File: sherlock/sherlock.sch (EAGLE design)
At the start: 24 parts, among them U3 XBEE-1B2, X1 2540-

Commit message: Fix all schematics to have a frame and be in quadrant I
Change-Id: I9709ffe2e940512e8f74172f888a837b658cad74
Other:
- moved on the sheet: BATTBUZZ, BATTCONN, C1, C2, C3, IC1, LED1, LED2, LED3, LED4, P1, P2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

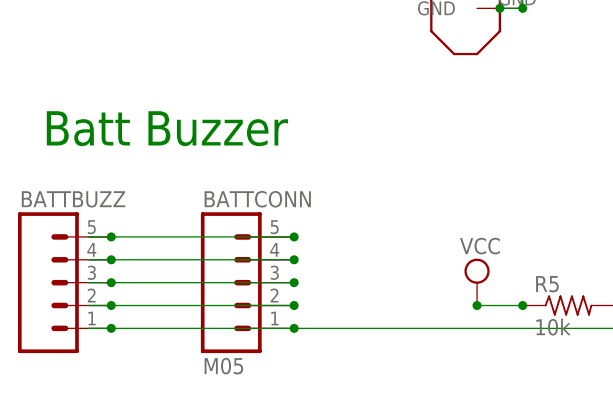
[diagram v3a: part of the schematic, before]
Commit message: Fixed XT60 connector in pie.lbr. Changed battery connector on sherlock to have 4 pins instead of 5. Replaced XT60 on sherlock, solenoid board, and grizzly bear with new version.
Change-Id: Ic4b688068eb477e37db8d2c4f2efb7678e25c5b6
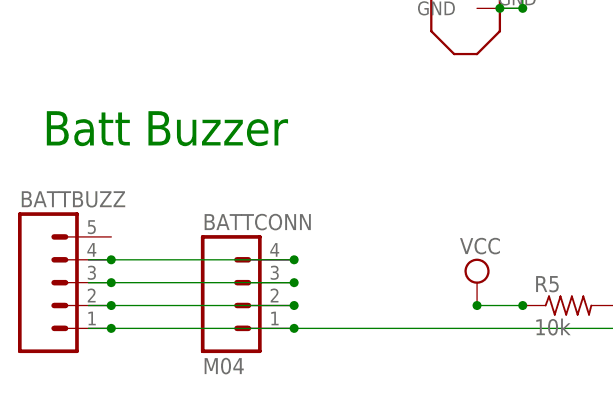
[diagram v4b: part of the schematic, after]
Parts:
- BATTCONN: value M05 -> M04; device pie:M05 -> pie:M04
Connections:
- removed net N$4: BATTBUZZ.5, BATTCONN.5
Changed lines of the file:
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@@
 <?xml version="1.0" encoding="utf-8"?>
 <!DOCTYPE eagle SYSTEM "eagle.dtd">
-<eagle version="6.2">
+<eagle version="6.3">
 <drawing>
 <settings>
@@
 </part>
 <part name="U$1" library="pie" deviceset="XT60CONNECTOR" device=""/>
-<part name="BATTCONN" library="pie" deviceset="M05" device=""/>
+<part name="BATTCONN" library="pie" deviceset="M04" device=""/>
 <part name="BATTBUZZ" library="SparkFun" deviceset="M05" device="PTH"/>
 <part name="R5" library="resistor" deviceset="R-US_" device="R0603" value="10k"/>
@@
 <instance part="X1" gate="-40" x="12.7" y="170.18" rot="R270"/>
 <instance part="U$1" gate="G$1" x="55.88" y="60.96" rot="R270"/>
-<instance part="BATTCONN" gate="G$1" x="35.56" y="22.86"/>
+<instance part="BATTCONN" gate="G$1" x="35.56" y="20.32"/>
 <instance part="BATTBUZZ" gate="G$1" x="12.7" y="20.32"/>
 <instance part="R5" gate="G$1" x="71.12" y="17.78"/>
@@
 </segment>
 </net>
-<net name="N$4" class="0">
-<segment>
-<pinref part="BATTBUZZ" gate="G$1" pin="5"/>
-<pinref part="BATTCONN" gate="G$1" pin="5"/>
-<wire x1="20.32" y1="25.4" x2="40.64" y2="25.4" width="0.1524" layer="91"/>
-<wire x1="20.32" y1="25.4" x2="17.78" y2="25.4" width="0.1524" layer="91"/>
-<junction x="20.32" y="25.4"/>
-<junction x="40.64" y="25.4"/>
-</segment>
-</net>

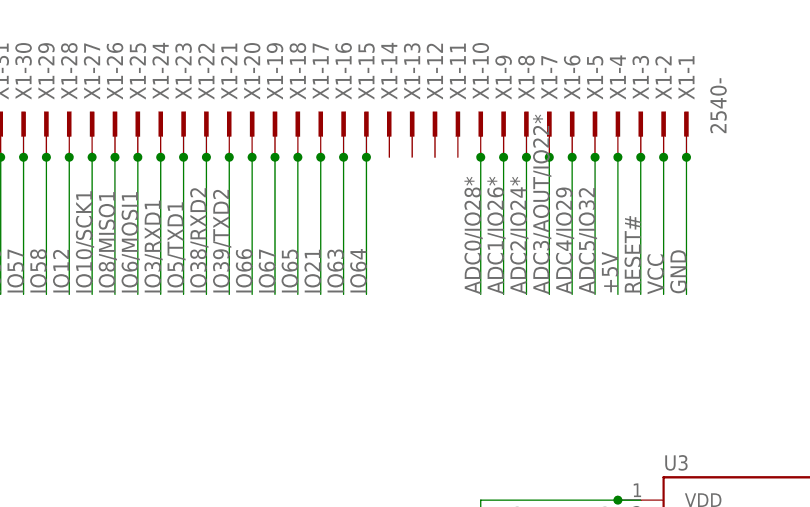
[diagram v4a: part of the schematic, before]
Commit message: Updated and fixed Sherlock and Watson to Rev C
- Changed RFID to SIMPLE, SPI to RFID on Watson.
- Added extra pin to RFID for interrupts (on Sherlock and Watson).

- Added 7-pin MTA connector to Eagle library.

- Added 0805 LED to Eagle library.

- Replaced LEDs on Sherlock to 0805 LEDs.

- Fixed version numbers and silkscreen on both boards.

DFM for SherlocK: https://www.freedfm.com/freedfm/0019486703397689/results/summary2.htm
DFM for Watson: https://www.freedfm.com/freedfm/0019486703397690/results/summary2.htm

Change-Id: Ib97956c76452f7ac388d76660bbab957bcb45fe9
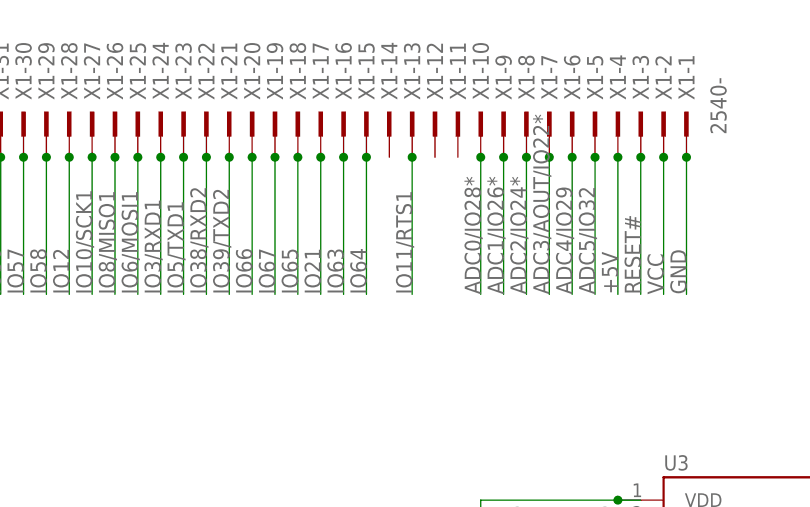
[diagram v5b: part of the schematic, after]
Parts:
- LED1, LED2, LED3, LED4: device pie:LED0603 -> pie:LED0805
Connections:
- net IO11/RTS1: now also X1-13.KL
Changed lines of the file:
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@@
 <part name="C1" library="rcl" deviceset="C-US" device="C0603" value=".1uF"/>
 <part name="IC1" library="pie" deviceset="78XXL" device=""/>
-<part name="LED4" library="pie" deviceset="LED" device="0603"/>
-<part name="LED1" library="pie" deviceset="LED" device="0603"/>
-<part name="LED2" library="pie" deviceset="LED" device="0603"/>
-<part name="LED3" library="pie" deviceset="LED" device="0603"/>
 <part name="X1" library="con-3m" deviceset="2540-" device="">
 <attribute name="OC_FARNELL" value="unknown"/>
@@
 <part name="FRAME1" library="pie" deviceset="FRAME-LETTER" device="">
 <attribute name="AUTHOR" value="Sahar M., Michael C., Sumita G."/>
-<attribute name="REVISION" value="A"/>
+<attribute name="REVISION" value="C"/>
 </part>
+<part name="LED4" library="pie" deviceset="LED" device="0805"/>
+<part name="LED1" library="pie" deviceset="LED" device="0805"/>
+<part name="LED2" library="pie" deviceset="LED" device="0805"/>
+<part name="LED3" library="pie" deviceset="LED" device="0805"/>
 </parts>
 <sheets>
@@
 <instance part="C1" gate="G$1" x="149.86" y="55.88"/>
 <instance part="IC1" gate="A" x="127" y="58.42"/>
-<instance part="LED4" gate="G$1" x="22.86" y="93.98"/>
-<instance part="LED1" gate="G$1" x="33.02" y="93.98"/>
-<instance part="LED2" gate="G$1" x="43.18" y="93.98"/>
-<instance part="LED3" gate="G$1" x="53.34" y="93.98"/>
 <instance part="X1" gate="-1" x="111.76" y="170.18" rot="R270"/>
 <instance part="X1" gate="-2" x="109.22" y="170.18" rot="R270"/>
@@
 <attribute name="AUTHOR" x="147.32" y="0" size="1.778" layer="96" display="off"/>
 </instance>
+<instance part="LED4" gate="G$1" x="22.86" y="93.98"/>
+<instance part="LED1" gate="G$1" x="33.02" y="93.98"/>
+<instance part="LED2" gate="G$1" x="43.18" y="93.98"/>
+<instance part="LED3" gate="G$1" x="53.34" y="93.98"/>
 </instances>
 <busses>
@@
 <pinref part="V1" gate="G$1" pin="VCC"/>
 <pinref part="C3" gate="G$1" pin="1"/>
+<junction x="60.96" y="104.14"/>
 <pinref part="LED1" gate="G$1" pin="A"/>
 <junction x="33.02" y="96.52"/>
-<junction x="60.96" y="104.14"/>
 </segment>
 <segment>
@@
 <pinref part="P3" gate="A" pin="28"/>
 </segment>
+<segment>
+<pinref part="X1" gate="-13" pin="KL"/>
+<wire x1="81.28" y1="165.1" x2="81.28" y2="149.86" width="0.1524" layer="91"/>
+<junction x="81.28" y="165.1"/>
+<label x="81.28" y="149.86" size="1.778" layer="95" rot="R90"/>
+</segment>
 </net>
 <net name="IO1/CTS1" class="0">
@@
 </segment>
 </net>
-<net name="N$1" class="0">
-<segment>
-<pinref part="R1" gate="G$1" pin="2"/>
-<pinref part="LED4" gate="G$1" pin="C"/>
-<junction x="22.86" y="88.9"/>
-</segment>
-</net>
-<net name="N$2" class="0">
-<segment>
-<pinref part="R2" gate="G$1" pin="2"/>
-<pinref part="LED1" gate="G$1" pin="C"/>
-<junction x="33.02" y="88.9"/>
-</segment>
-</net>
-<net name="N$3" class="0">
-<segment>
-<pinref part="R3" gate="G$1" pin="2"/>
-<pinref part="LED2" gate="G$1" pin="C"/>
-<junction x="43.18" y="88.9"/>
-</segment>
-</net>
-<net name="N$8" class="0">
-<segment>
-<pinref part="R4" gate="G$1" pin="2"/>
-<pinref part="LED3" gate="G$1" pin="C"/>
-<junction x="53.34" y="88.9"/>
-</segment>
-</net>
 <net name="SDA0/IO33*" class="0">
 <segment>
@@
 </segment>
 </net>
+<net name="N$1" class="0">
+<segment>
+<pinref part="R1" gate="G$1" pin="2"/>
+<pinref part="LED4" gate="G$1" pin="C"/>
+<junction x="22.86" y="88.9"/>
+</segment>
+</net>
+<net name="N$2" class="0">
+<segment>
+<pinref part="R2" gate="G$1" pin="2"/>
+<pinref part="LED1" gate="G$1" pin="C"/>
+<junction x="33.02" y="88.9"/>
+</segment>
+</net>
+<net name="N$3" class="0">
+<segment>
+<pinref part="R3" gate="G$1" pin="2"/>
+<pinref part="LED2" gate="G$1" pin="C"/>
+<junction x="43.18" y="88.9"/>
+</segment>
+</net>
+<net name="N$4" class="0">
+<segment>
+<pinref part="R4" gate="G$1" pin="2"/>
+<pinref part="LED3" gate="G$1" pin="C"/>
+<junction x="53.34" y="88.9"/>
+</segment>
+</net>
